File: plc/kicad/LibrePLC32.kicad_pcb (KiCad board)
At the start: 4 copper layers, 274 parts, among them CN1 DB128V-5.08-2P-GN-S, CN10 DB128V-5.08-6P-GN-S, CN11 DB2ERC-5.08-4P, CN12 DB2ERC-5.08-4P, CN2 DB128V-5.08-2P-GN-S, CN3 DB128V-5.08-2P-GN-S, CN4 DB128V-5.08-2P-GN-S, CN5 DB128V-5.08-2P-GN-S, CN6 DB128V-5.08-2P-GN-S, CN7 DB128V-5.08-2P-GN-S, CN8 DB128V-5.08-2P-GN-S, CN9 DB128V-5.08-2P-GN-S, J2 Conn_01x04_Pin, J3 Conn_01x02_Pin, Q1 AO3400A, Q2 AO3400A, Q3 L8050QLT1G, Q4 L8050QLT1G, Q5 BSS138LT1G, Q6 CSD19537Q3, SW1 TSD003B08026A03, SW2 TSD003B08026A03, SW3 TSD003B08026A03, SW4 MSK12C02, SW5 MSK12C02, U1 TCA9535PWR, U10 ESP32-S3-MINI-1U, U11 BS-0601-SK-4W, U12 AHT20_C2757850, U13 CP2102N-A02-GQFN28R, U14 LMR16006XDDCR, U15 TPS7A5201QRGRRQ1, U16 TPS26630RGER, U18 TCAN337DR, U19 THVD1450DR, U2 TPS272C45DRHFR, U20 W5500, U21 TPS54560BDDAR, U3 TPS272C45DRHFR, U4 ADS1115IDGSR, U5 LTV-814S-TA1-A, U6 LTV-814S-TA1-A, U7 LTV-814S-TA1-A, U8 LTV-814S-TA1-A, U9 RV-3028-C7, X1 X322525MRB4SI

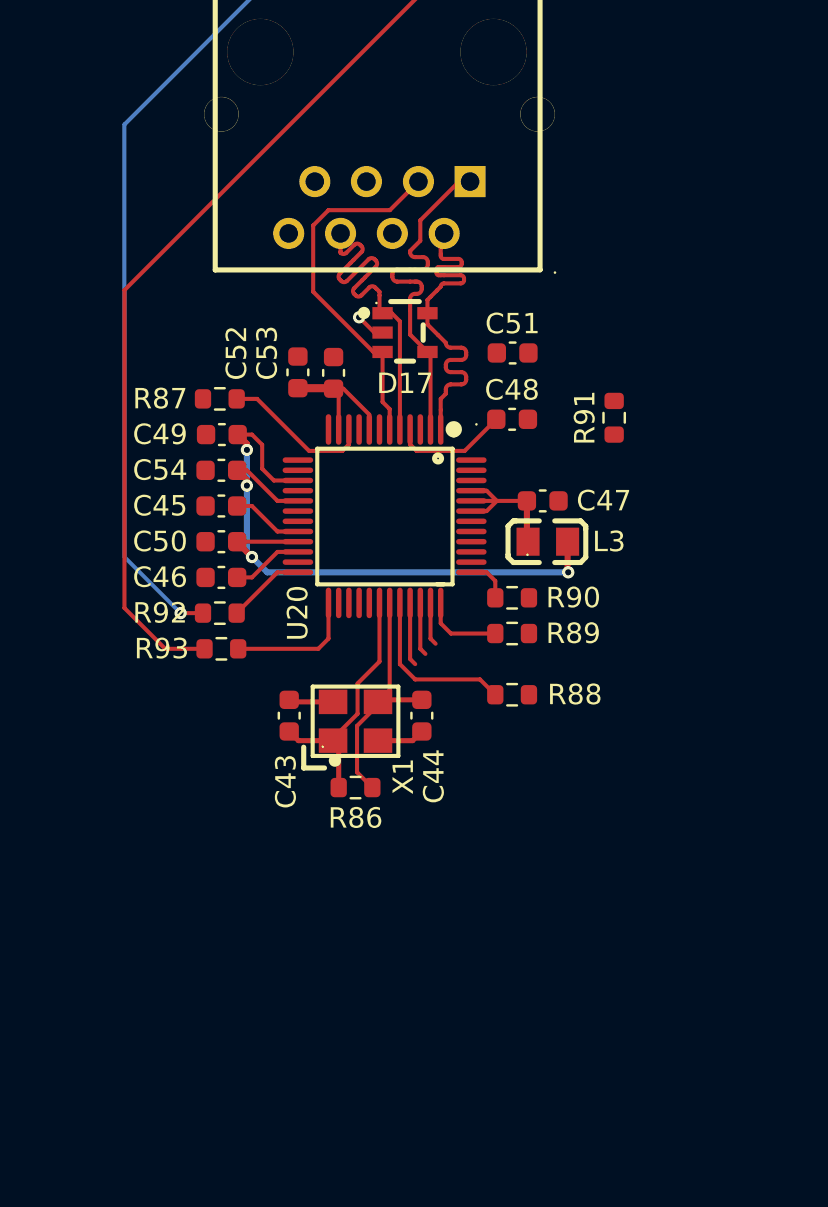
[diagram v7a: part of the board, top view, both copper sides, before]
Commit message: Updated W5500 PCB Placement
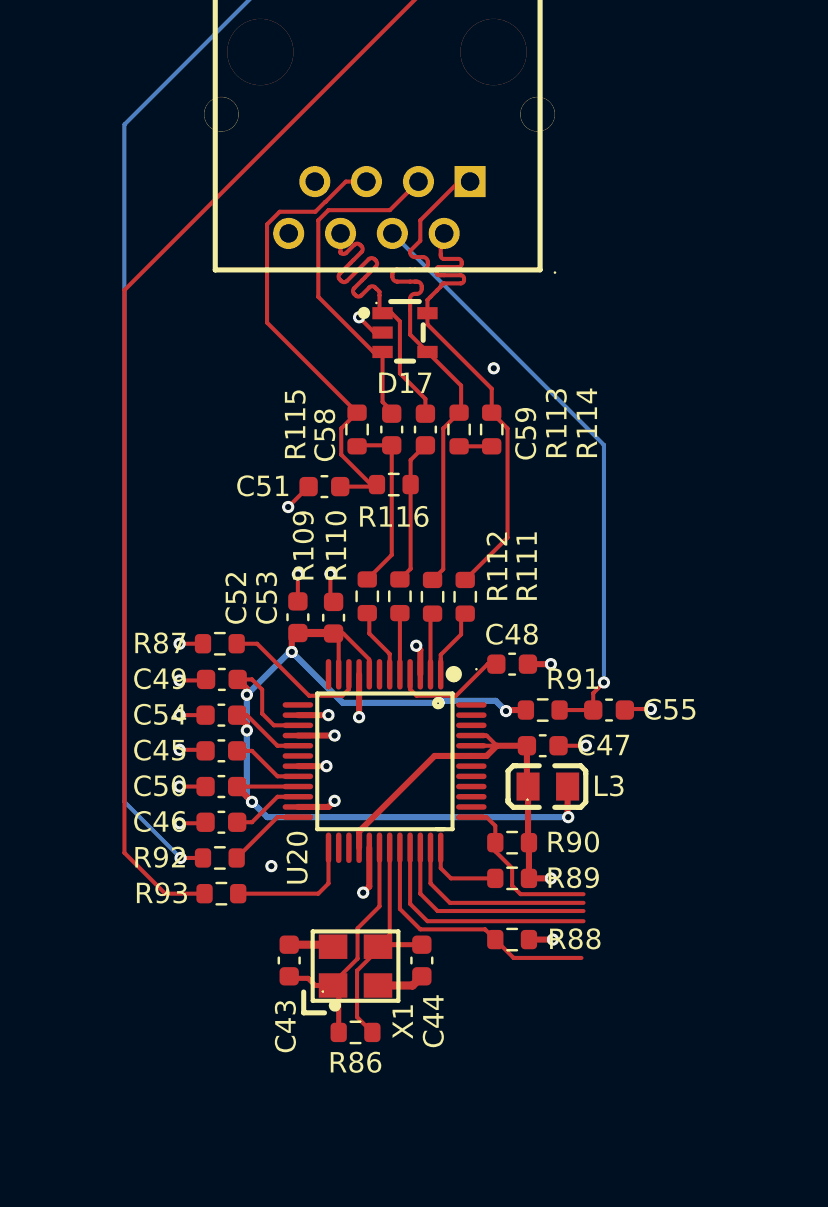
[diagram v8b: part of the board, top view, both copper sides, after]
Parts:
- added C55: 22n, Capacitor_SMD:C_0603_1608Metric, F.Cu at (191.2, -68.2)
- added C58: 6.8n, Capacitor_SMD:C_0603_1608Metric, F.Cu at (180.6, -82.0)
- added C59: 6.8n, Capacitor_SMD:C_0603_1608Metric, F.Cu at (182.2, -82.0)
- added R109: 33, Resistor_SMD:R_0603_1608Metric, F.Cu at (179.4, -73.8)
- added R110: 33, Resistor_SMD:R_0603_1608Metric, F.Cu at (181.0, -73.8)
- added R111: 33, Resistor_SMD:R_0603_1608Metric, F.Cu at (184.2, -73.8)
- added R112: 33, Resistor_SMD:R_0603_1608Metric, F.Cu at (182.6, -73.8)
- added R113: 49, Resistor_SMD:R_0603_1608Metric, F.Cu at (183.9, -82.0)
- added R114: 49, Resistor_SMD:R_0603_1608Metric, F.Cu at (185.5, -82.0)
- added R115: 49, Resistor_SMD:R_0603_1608Metric, F.Cu at (178.9, -82.0)
- added R116: 49, Resistor_SMD:R_0603_1608Metric, F.Cu at (180.7, -79.3)
- C51: value 100n -> 10n
- R91: value 0 -> 10
- moved R91 14.7 mm to (188.0, -68.2), turned to 0 degrees
- moved C45 12.0 mm to (172.2, -66.2)
- moved C46 12.0 mm to (172.2, -62.8)
- moved C47 12.0 mm to (188.0, -66.5)
- moved C48 12.0 mm to (186.5, -70.5)
- moved C49 12.0 mm to (172.3, -69.8)
- moved C50 12.0 mm to (172.2, -64.5)
- moved C52 12.0 mm to (176.0, -72.8)
- moved C53 12.0 mm to (177.8, -72.8)
- moved C54 12.0 mm to (172.2, -68.0)
- moved L3 12.0 mm to (188.2, -64.5)
- moved R86 12.0 mm to (178.8, -52.5)
- moved R87 12.0 mm to (172.2, -71.5)
- moved R88 12.0 mm to (186.5, -57.0)
- moved R89 12.0 mm to (186.5, -60.0)
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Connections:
- R91 pad 1: +3V3 -> +3V3A
- U20 pad 1: /Ethernet/RJ45_TX- -> /Ethernet/ETH_TX-
- U20 pad 2: /Ethernet/RJ45_TX+ -> /Ethernet/ETH_TX+
- U20 pad 5: /Ethernet/RJ45_RX- -> /Ethernet/ETH_RX-
- U20 pad 6: /Ethernet/RJ45_RX+ -> /Ethernet/ETH_RX+
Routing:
- net /Ethernet/RJ45_TCT: track 0.00 -> 29.5 mm, vias 0 -> 1
- net GND: track 69.0 -> 97.2 mm, vias 57 -> 78
- net /Ethernet/RJ45_RCT: track 0.00 -> 23.4 mm
- net +3V3A: track 49.4 -> 68.2 mm, vias 4 -> 7
- net +3V3: track 42.8 -> 60.4 mm, vias 3 -> 5
- net Net-(RJ1-LED(Y)_K): track 38.1 -> 50.1 mm
- net Net-(RJ1-LED(G)_K): track 43.8 -> 55.8 mm
- net /Ethernet/RXP: track 0.00 -> 8.79 mm
- net /Ethernet/SPI_SCLK: track 3.10 -> 11.6 mm
- net /Ethernet/RJ45_TX+: track 17.8 -> 26.3 mm
- net /Ethernet/SPI_MISO: track 2.60 -> 10.6 mm
- net /Ethernet/SPI_MOSI: track 2.10 -> 9.64 mm
- net /Ethernet/RXN: track 0.00 -> 7.09 mm
- net /Ethernet/RJ45_TX-: track 17.7 -> 24.0 mm
- net /Ethernet/~{ETH_RST}: track 2.43 -> 8.55 mm
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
